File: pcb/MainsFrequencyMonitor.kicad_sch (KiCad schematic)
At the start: 26 parts, among them J1 L_{in}, J2 N_{in}, J3 Serial, J4 I2C, SW1 RST, SW2 BOOT, U1 EL357N(C), U2 ESP32-WROOM-32

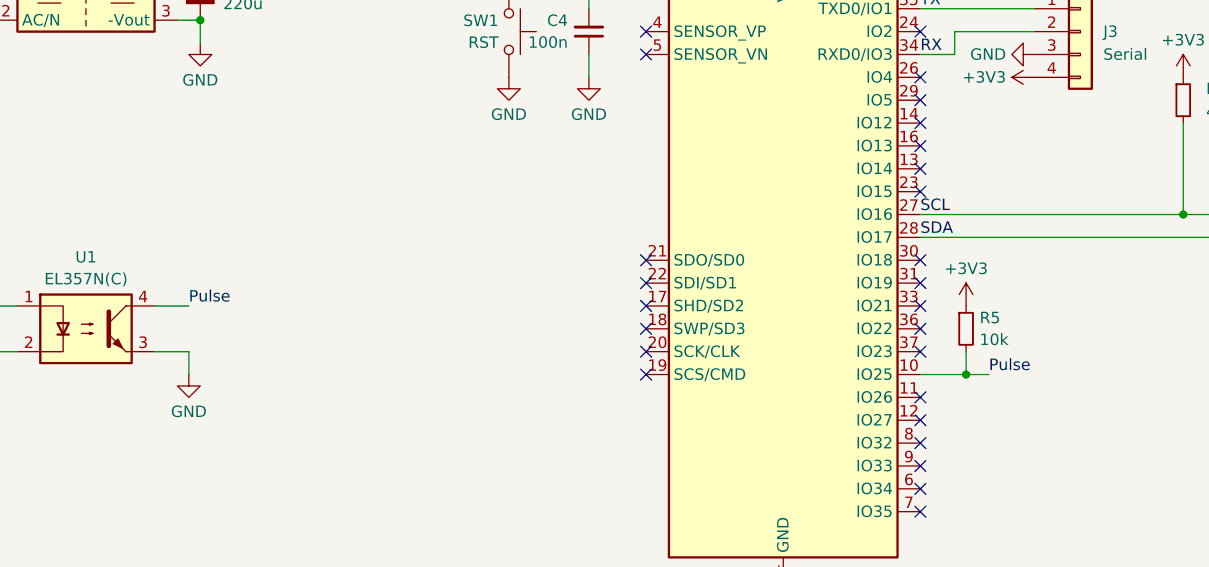
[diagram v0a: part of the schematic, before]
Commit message: fix: add capacitor to optocouplers output
Output of the optocoupler was not a smooth square wave form but had some voltage spikes. Adding a 100nF capacitor to the output solved this.
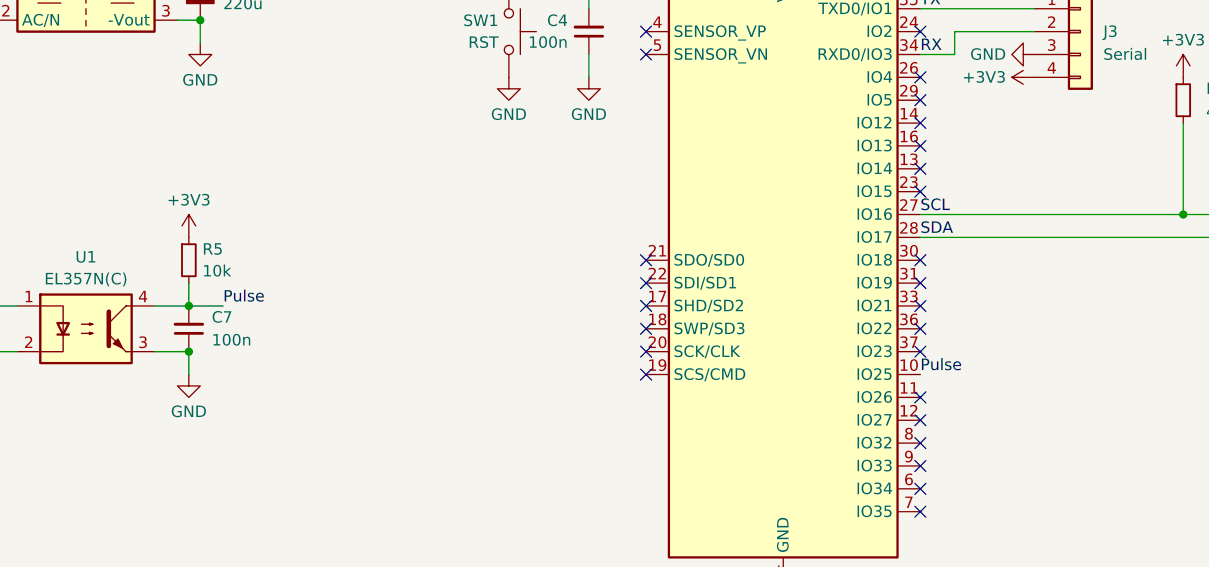
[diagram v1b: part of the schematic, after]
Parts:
- added C7: 100n, Capacitor_SMD:C_0603_1608Metric_Pad1.08x0.95mm_HandSolder, symbol Device:C_Small
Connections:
- net GND: now also C7.1
- net Pulse: now also C7.2
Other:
- moved on the sheet: R5
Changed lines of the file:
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@@
 	)
 	(junction
-		(at 201.93 110.49)
+		(at 115.57 107.95)
 		(diameter 0)
 		(color 0 0 0 0)
@@
 	)
 	(junction
+		(at 115.57 102.87)
+		(diameter 0)
+		(color 0 0 0 0)
+	)
+	(junction
 		(at 204.47 67.31)
 		(diameter 0)
@@
 	(wire
 		(pts
-			(xy 201.93 107.95) (xy 201.93 110.49)
+			(xy 115.57 100.33) (xy 115.57 102.87)
 		)
 		(stroke
@@
 	(wire
 		(pts
+			(xy 115.57 102.87) (xy 119.38 102.87)
+		)
+		(stroke
+			(width 0)
+			(type default)
+		)
+	)
+	(wire
+		(pts
 			(xy 52.07 66.04) (xy 54.61 66.04)
 		)
@@
 	(wire
 		(pts
-			(xy 201.93 110.49) (xy 196.85 110.49)
-		)
-		(stroke
-			(width 0)
-			(type default)
-		)
-	)
-	(wire
-		(pts
 			(xy 43.18 76.2) (xy 58.42 76.2)
 		)
@@
 	(wire
 		(pts
-			(xy 204.47 110.49) (xy 201.93 110.49)
-		)
-		(stroke
-			(width 0)
-			(type default)
-		)
-	)
-	(wire
-		(pts
 			(xy 111.76 107.95) (xy 115.57 107.95)
 		)
@@
 	)
 	(label "Pulse"
-		(at 204.47 110.49 0)
+		(at 196.85 110.49 0)
 		(fields_autoplaced yes)
 		(effects
@@
 	)
 	(label "Pulse"
-		(at 115.57 102.87 0)
+		(at 119.38 102.87 0)
 		(fields_autoplaced yes)
 		(effects
@@
 	)
 	(symbol
+		(lib_id "Device:C_Small")
+		(at 115.57 105.41 180)
+		(unit 1)
+		(exclude_from_sim no)
+		(in_bom yes)
+		(on_board yes)
+		(dnp no)
+		(fields_autoplaced yes)
+		(property "Reference" "C7"
+			(at 118.11 104.1335 0)
+			(effects
+				(font
+					(size 1.27 1.27)
+				)
+				(justify right)
+			)
+		)
+		(property "Value" "100n"
+			(at 118.11 106.6735 0)
+			(effects
+				(font
+					(size 1.27 1.27)
+				)
+				(justify right)
+			)
+		)
+		(property "Footprint" "Capacitor_SMD:C_0603_1608Metric_Pad1.08x0.95mm_HandSolder"
+			(at 115.57 105.41 0)
+			(effects
+				(font
+					(size 1.27 1.27)
+				)
+				(hide yes)
+			)
+		)
+		(property "Datasheet" "~"
+			(at 115.57 105.41 0)
+			(effects
+				(font
+					(size 1.27 1.27)
+				)
+				(hide yes)
+			)
+		)
+		(property "Description" "Unpolarized capacitor, small symbol"
+			(at 115.57 105.41 0)
+			(effects
+				(font
+					(size 1.27 1.27)
+				)
+				(hide yes)
+			)
+		)
+		(property "LCSC" "C14663"
+			(at 115.57 105.41 0)
+			(effects
+				(font
+					(size 1.27 1.27)
+				)
+				(hide yes)
+			)
+		)
+		(pin "2"
+		)
+		(pin "1"
+		)
+		(instances
+			(project "MainsFrequencyMonitor"
+				(path "/f5b99735-4766-4376-b536-e49ae93be466"
+					(reference "C7")
+					(unit 1)
+				)
+			)
+		)
+	)
+	(symbol
 		(lib_id "power:+3V3")
 		(at 204.47 57.15 0)
@@
 	(symbol
 		(lib_id "Device:R_Small")
-		(at 201.93 105.41 0)
+		(at 115.57 97.79 0)
 		(unit 1)
 		(exclude_from_sim no)
@@
 		(fields_autoplaced yes)
 		(property "Reference" "R5"
-			(at 203.4286 104.1978 0)
+			(at 117.0686 96.5778 0)
 			(effects
 				(font
@@
 		)
 		(property "Value" "10k"
-			(at 203.4286 106.6221 0)
+			(at 117.0686 99.0021 0)
 			(effects
 				(font
@@
 		)
 		(property "Footprint" "Resistor_SMD:R_0603_1608Metric_Pad0.98x0.95mm_HandSolder"
-			(at 201.93 105.41 0)
+			(at 115.57 97.79 0)
 			(effects
 				(font
@@
 		)
 		(property "Datasheet" "~"
-			(at 201.93 105.41 0)
+			(at 115.57 97.79 0)
 			(effects
 				(font
@@
 		)
 		(property "Description" "Resistor, small symbol"
-			(at 201.93 105.41 0)
+			(at 115.57 97.79 0)
 			(effects
 				(font
@@
 		)
 		(property "LCSC" "C25804"
-			(at 201.93 105.41 0)
+			(at 115.57 97.79 0)
 			(effects
 				(font
@@
 	(symbol
 		(lib_id "power:+3V3")
-		(at 201.93 102.87 0)
+		(at 115.57 95.25 0)
 		(unit 1)
 		(exclude_from_sim no)
@@
 		(fields_autoplaced yes)
 		(property "Reference" "#PWR017"
-			(at 201.93 106.68 0)
+			(at 115.57 99.06 0)
 			(effects
 				(font
@@
 		)
 		(property "Value" "+3V3"
-			(at 201.93 98.7369 0)
+			(at 115.57 91.1169 0)
 			(effects
 				(font
@@
 		)
 		(property "Footprint" ""
-			(at 201.93 102.87 0)
+			(at 115.57 95.25 0)
 			(effects
 				(font
@@
 		)
 		(property "Datasheet" ""
-			(at 201.93 102.87 0)
+			(at 115.57 95.25 0)
 			(effects
 				(font
@@
 		)
 		(property "Description" "Power symbol creates a global label with name \"+3V3\""
-			(at 201.93 102.87 0)
+			(at 115.57 95.25 0)
 			(effects
 				(font
